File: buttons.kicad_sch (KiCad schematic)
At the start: 91 parts, among them SW1 TC002-N11AS2XT-RGB, SW10 TC002-N11AS2XT-RGB, SW11 TC002-N11AS2XT-RGB, SW12 TC002-N11AS2XT-RGB, SW13 TC002-N11AS2XT-RGB, SW2 TC002-N11AS2XT-RGB, SW3 TC002-N11AS2XT-RGB, SW4 TC002-N11AS2XT-RGB, SW5 TC002-N11AS2XT-RGB, SW6 TC002-N11AS2XT-RGB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

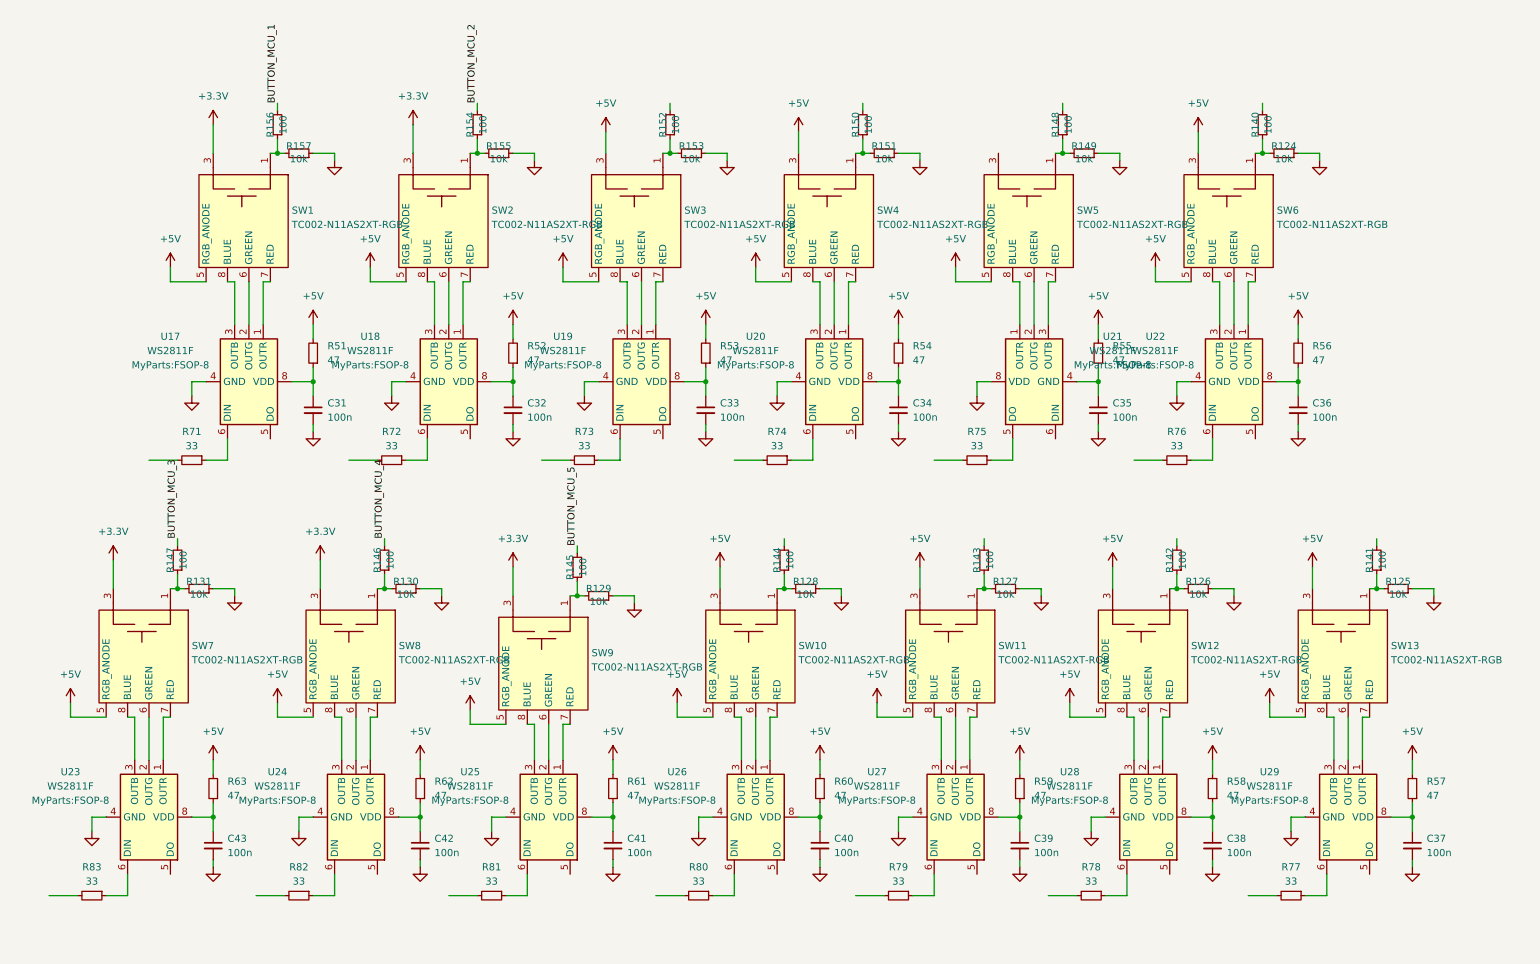
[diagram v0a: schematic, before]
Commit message: rename symbol & footprint libs
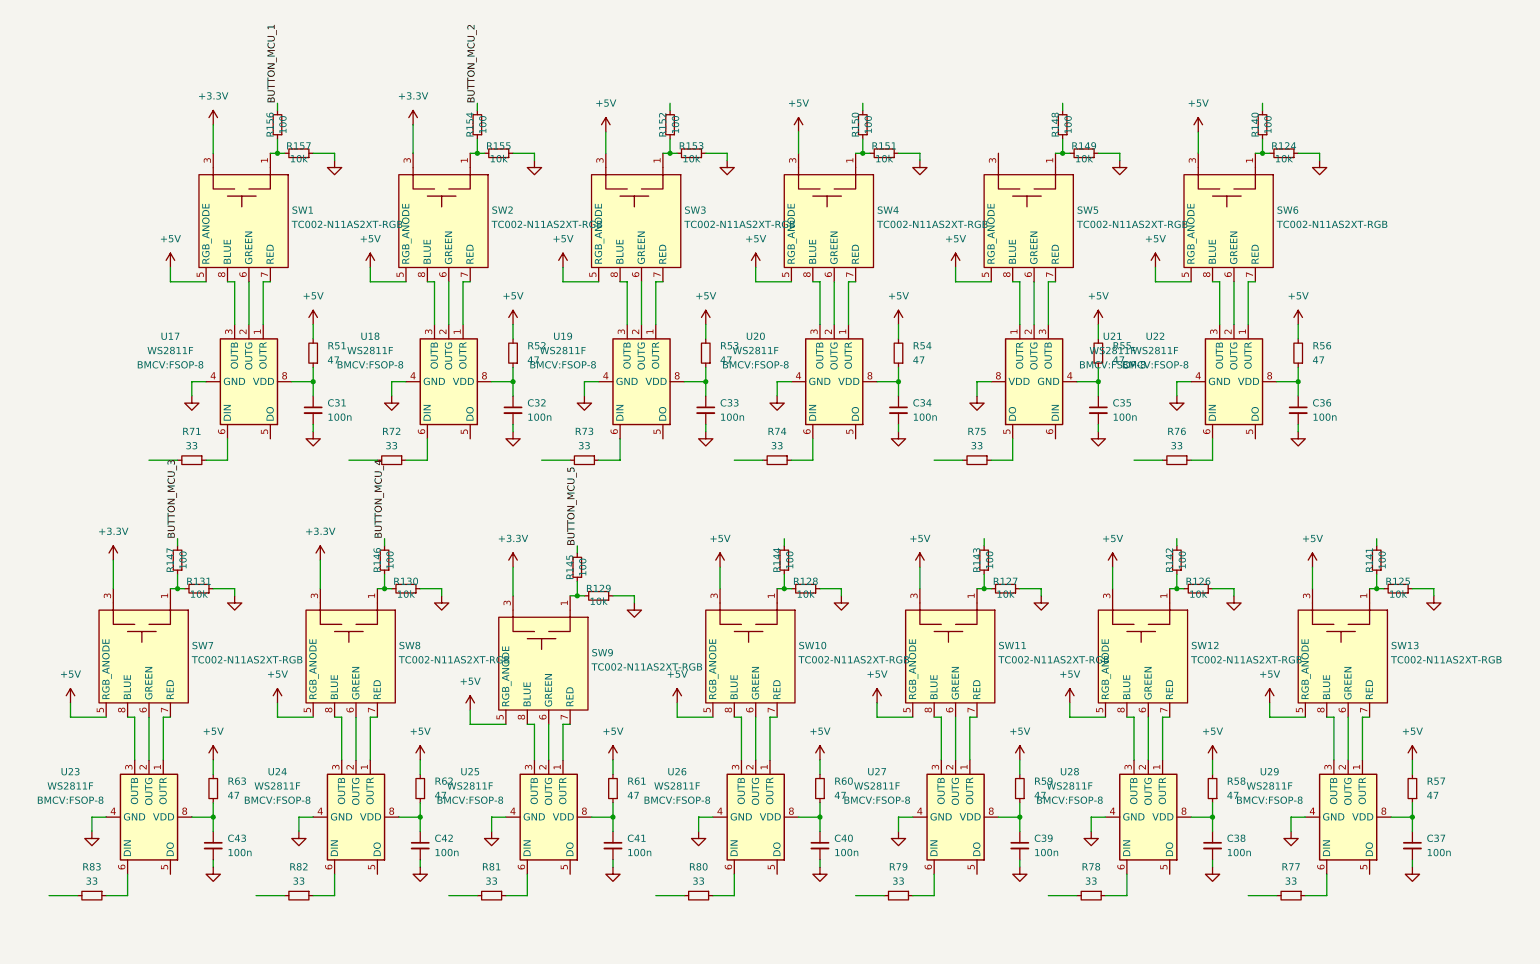
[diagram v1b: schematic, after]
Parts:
- SW1, SW10, SW11, SW12, SW13, SW2, SW3, SW4, SW5, SW6, SW7, SW8, SW9: footprint MyParts:TC002-N11AXXX-RGB -> BMCV:TC002-N11AXXX-RGB; symbol MySymbols:TC002-N11BXXX-RGB -> BMCV:TC002-N11BXXX-RGB
- U17, U18, U19, U20, U21, U22, U23, U24, U25, U26, U27, U28, U29: footprint MyParts:FSOP-8 -> BMCV:FSOP-8; symbol MySymbols:WS2811 -> BMCV:WS2811
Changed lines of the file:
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@@
 	)
 	(symbol
-		(lib_id "MySymbols:WS2811")
+		(lib_id "BMCV:WS2811")
 		(at 110.49 146.05 270)
 		(mirror x)
@@
 			)
 		)
-		(property "Footprint" "MyParts:FSOP-8"
+		(property "Footprint" "BMCV:FSOP-8"
 			(at 96.52 143.0938 90)
 			(effects
@@
 	)
 	(symbol
-		(lib_id "MySymbols:TC002-N11BXXX-RGB")
+		(lib_id "BMCV:TC002-N11BXXX-RGB")
 		(at 215.9 116.84 270)
 		(unit 1)
@@
 			)
 		)
-		(property "Footprint" "MyParts:TC002-N11AXXX-RGB"
+		(property "Footprint" "BMCV:TC002-N11AXXX-RGB"
 			(at 215.9 116.84 0)
 			(effects
@@
 	)
 	(symbol
-		(lib_id "MySymbols:TC002-N11BXXX-RGB")
+		(lib_id "BMCV:TC002-N11BXXX-RGB")
 		(at 251.46 116.84 270)
 		(unit 1)
@@
 			)
 		)
-		(property "Footprint" "MyParts:TC002-N11AXXX-RGB"
+		(property "Footprint" "BMCV:TC002-N11AXXX-RGB"
 			(at 251.46 116.84 0)
 			(effects
@@
 	)
 	(symbol
-		(lib_id "MySymbols:WS2811")
+		(lib_id "BMCV:WS2811")
 		(at 147.32 146.05 270)
 		(mirror x)
@@
 			)
 		)
-		(property "Footprint" "MyParts:FSOP-8"
+		(property "Footprint" "BMCV:FSOP-8"
 			(at 133.35 143.0938 90)
 			(effects
@@
 	)
 	(symbol
-		(lib_id "MySymbols:TC002-N11BXXX-RGB")
+		(lib_id "BMCV:TC002-N11BXXX-RGB")
 		(at 160.02 39.37 270)
 		(unit 1)
@@
 			)
 		)
-		(property "Footprint" "MyParts:TC002-N11AXXX-RGB"
+		(property "Footprint" "BMCV:TC002-N11AXXX-RGB"
 			(at 160.02 39.37 0)
 			(effects
@@
 	)
 	(symbol
-		(lib_id "MySymbols:TC002-N11BXXX-RGB")
+		(lib_id "BMCV:TC002-N11BXXX-RGB")
 		(at 55.88 39.37 270)
 		(unit 1)
@@
 			)
 		)
-		(property "Footprint" "MyParts:TC002-N11AXXX-RGB"
+		(property "Footprint" "BMCV:TC002-N11AXXX-RGB"
 			(at 55.88 39.37 0)
 			(effects
@@
 	)
 	(symbol
-		(lib_id "MySymbols:TC002-N11BXXX-RGB")
+		(lib_id "BMCV:TC002-N11BXXX-RGB")
 		(at 195.58 39.37 270)
 		(unit 1)
@@
 			)
 		)
-		(property "Footprint" "MyParts:TC002-N11AXXX-RGB"
+		(property "Footprint" "BMCV:TC002-N11AXXX-RGB"
 			(at 195.58 39.37 0)
 			(effects
@@
 	)
 	(symbol
-		(lib_id "MySymbols:WS2811")
+		(lib_id "BMCV:WS2811")
 		(at 39.37 146.05 270)
 		(mirror x)
@@
 			)
 		)
-		(property "Footprint" "MyParts:FSOP-8"
+		(property "Footprint" "BMCV:FSOP-8"
 			(at 25.4 143.0938 90)
 			(effects
@@
 	)
 	(symbol
-		(lib_id "MySymbols:TC002-N11BXXX-RGB")
+		(lib_id "BMCV:TC002-N11BXXX-RGB")
 		(at 146.05 116.84 270)
 		(unit 1)
@@
 			)
 		)
-		(property "Footprint" "MyParts:TC002-N11AXXX-RGB"
+		(property "Footprint" "BMCV:TC002-N11AXXX-RGB"
 			(at 146.05 116.84 0)
 			(effects
@@
 	)
 	(symbol
-		(lib_id "MySymbols:TC002-N11BXXX-RGB")
+		(lib_id "BMCV:TC002-N11BXXX-RGB")
 		(at 38.1 116.84 270)
 		(unit 1)
@@
 			)
 		)
-		(property "Footprint" "MyParts:TC002-N11AXXX-RGB"
+		(property "Footprint" "BMCV:TC002-N11AXXX-RGB"
 			(at 38.1 116.84 0)
 			(effects
@@
 	)
 	(symbol
-		(lib_id "MySymbols:WS2811")
+		(lib_id "BMCV:WS2811")
 		(at 217.17 146.05 270)
 		(mirror x)
@@
 			)
 		)
-		(property "Footprint" "MyParts:FSOP-8"
+		(property "Footprint" "BMCV:FSOP-8"
 			(at 203.2 143.0938 90)
 			(effects
@@
 	)
 	(symbol
-		(lib_id "MySymbols:TC002-N11BXXX-RGB")
+		(lib_id "BMCV:TC002-N11BXXX-RGB")
 		(at 74.93 116.84 270)
 		(unit 1)
@@
 			)
 		)
-		(property "Footprint" "MyParts:TC002-N11AXXX-RGB"
+		(property "Footprint" "BMCV:TC002-N11AXXX-RGB"
 			(at 74.93 116.84 0)
 			(effects
@@
 	)
 	(symbol
-		(lib_id "MySymbols:TC002-N11BXXX-RGB")
+		(lib_id "BMCV:TC002-N11BXXX-RGB")
 		(at 125.73 39.37 270)
 		(unit 1)
@@
 			)
 		)
-		(property "Footprint" "MyParts:TC002-N11AXXX-RGB"
+		(property "Footprint" "BMCV:TC002-N11AXXX-RGB"
 			(at 125.73 39.37 0)
 			(effects
@@
 	)
 	(symbol
-		(lib_id "MySymbols:WS2811")
+		(lib_id "BMCV:WS2811")
 		(at 161.29 68.58 270)
 		(mirror x)
@@
 			)
 		)
-		(property "Footprint" "MyParts:FSOP-8"
+		(property "Footprint" "BMCV:FSOP-8"
 			(at 147.32 65.6238 90)
 			(effects
@@
 	)
 	(symbol
-		(lib_id "MySymbols:WS2811")
+		(lib_id "BMCV:WS2811")
 		(at 92.71 68.58 270)
 		(mirror x)
@@
 			)
 		)
-		(property "Footprint" "MyParts:FSOP-8"
+		(property "Footprint" "BMCV:FSOP-8"
 			(at 78.74 65.6238 90)
 			(effects
@@
 	)
 	(symbol
-		(lib_id "MySymbols:TC002-N11BXXX-RGB")
+		(lib_id "BMCV:TC002-N11BXXX-RGB")
 		(at 181.61 116.84 270)
 		(unit 1)
@@
 			)
 		)
-		(property "Footprint" "MyParts:TC002-N11AXXX-RGB"
+		(property "Footprint" "BMCV:TC002-N11AXXX-RGB"
 			(at 181.61 116.84 0)
 			(effects
@@
 	)
 	(symbol
-		(lib_id "MySymbols:WS2811")
+		(lib_id "BMCV:WS2811")
 		(at 252.73 146.05 270)
 		(mirror x)
@@
 			)
 		)
-		(property "Footprint" "MyParts:FSOP-8"
+		(property "Footprint" "BMCV:FSOP-8"
 			(at 238.76 143.0938 90)
 			(effects
@@
 	)
 	(symbol
-		(lib_id "MySymbols:WS2811")
+		(lib_id "BMCV:WS2811")
 		(at 196.85 68.58 90)
 		(unit 1)
@@
 			)
 		)
-		(property "Footprint" "MyParts:FSOP-8"
+		(property "Footprint" "BMCV:FSOP-8"
 			(at 210.82 65.6238 90)
 			(effects
@@
 	)
 	(symbol
-		(lib_id "MySymbols:WS2811")
+		(lib_id "BMCV:WS2811")
 		(at 127 68.58 270)
 		(mirror x)
@@
 			)
 		)
-		(property "Footprint" "MyParts:FSOP-8"
+		(property "Footprint" "BMCV:FSOP-8"
 			(at 113.03 65.6238 90)
 			(effects
@@
 	)
 	(symbol
-		(lib_id "MySymbols:WS2811")
+		(lib_id "BMCV:WS2811")
 		(at 57.15 68.58 270)
 		(mirror x)
@@
 			)
 		)
-		(property "Footprint" "MyParts:FSOP-8"
+		(property "Footprint" "BMCV:FSOP-8"
 			(at 43.18 65.6238 90)
 			(effects
@@
 	)
 	(symbol
-		(lib_id "MySymbols:TC002-N11BXXX-RGB")
+		(lib_id "BMCV:TC002-N11BXXX-RGB")
 		(at 231.14 39.37 270)
 		(unit 1)
@@
 			)
 		)
-		(property "Footprint" "MyParts:TC002-N11AXXX-RGB"
+		(property "Footprint" "BMCV:TC002-N11AXXX-RGB"
 			(at 231.14 39.37 0)
 			(effects
@@
 	)
 	(symbol
-		(lib_id "MySymbols:WS2811")
+		(lib_id "BMCV:WS2811")
 		(at 76.2 146.05 270)
 		(mirror x)
@@
 			)
 		)
-		(property "Footprint" "MyParts:FSOP-8"
+		(property "Footprint" "BMCV:FSOP-8"
 			(at 62.23 143.0938 90)
 			(effects
@@
 	)
 	(symbol
-		(lib_id "MySymbols:TC002-N11BXXX-RGB")
+		(lib_id "BMCV:TC002-N11BXXX-RGB")
 		(at 109.22 118.11 270)
 		(unit 1)
@@
 			)
 		)
-		(property "Footprint" "MyParts:TC002-N11AXXX-RGB"
+		(property "Footprint" "BMCV:TC002-N11AXXX-RGB"
 			(at 109.22 118.11 0)
 			(effects
@@
 	)
 	(symbol
-		(lib_id "MySymbols:TC002-N11BXXX-RGB")
+		(lib_id "BMCV:TC002-N11BXXX-RGB")
 		(at 91.44 39.37 270)
 		(unit 1)
@@
 			)
 		)
-		(property "Footprint" "MyParts:TC002-N11AXXX-RGB"
+		(property "Footprint" "BMCV:TC002-N11AXXX-RGB"
 			(at 91.44 39.37 0)
 			(effects
@@
 	)
 	(symbol
-		(lib_id "MySymbols:WS2811")
+		(lib_id "BMCV:WS2811")
 		(at 182.88 146.05 270)
 		(mirror x)
@@
 			)
 		)
-		(property "Footprint" "MyParts:FSOP-8"
+		(property "Footprint" "BMCV:FSOP-8"
 			(at 168.91 143.0938 90)
 			(effects
@@
 	)
 	(symbol
-		(lib_id "MySymbols:WS2811")
+		(lib_id "BMCV:WS2811")
 		(at 232.41 68.58 270)
 		(mirror x)
@@
 			)
 		)
-		(property "Footprint" "MyParts:FSOP-8"
+		(property "Footprint" "BMCV:FSOP-8"
 			(at 218.44 65.6238 90)
 			(effects

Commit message: Routing WIP
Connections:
- net +3.3V: now also SW11.3, SW11.4, SW12.3, SW12.4, SW13.3, SW13.4, SW5.3, SW5.4, SW6.3, SW6.4; no longer SW1.3, SW1.4, SW2.3, SW2.4, SW7.3, SW7.4, SW8.3, SW8.4, SW9.3, SW9.4
- net +5V: now also SW1.3, SW1.4, SW2.3, SW2.4, SW7.3, SW7.4, SW8.3, SW8.4, SW9.3, SW9.4; no longer SW11.3, SW11.4, SW12.3, SW12.4, SW13.3, SW13.4, SW6.3, SW6.4
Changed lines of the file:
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@@
 	(wire
 		(pts
+			(xy 190.5 24.13) (xy 190.5 27.94)
+		)
+		(stroke
+			(width 0)
+			(type default)
+		)
+	)
+	(wire
+		(pts
 			(xy 104.14 66.04) (xy 104.14 68.58)
 		)
@@
 	(symbol
 		(lib_id "PCM_4ms_Power-symbol:+3.3V")
-		(at 104.14 101.6 0)
+		(at 210.82 101.6 0)
 		(unit 1)
 		(exclude_from_sim no)
@@
 		(fields_autoplaced yes)
 		(property "Reference" "#PWR0224"
-			(at 104.14 105.41 0)
+			(at 210.82 105.41 0)
 			(effects
 				(font
@@
 		)
 		(property "Value" "+3.3V"
-			(at 104.14 96.52 0)
+			(at 210.82 96.52 0)
 			(effects
 				(font
@@
 		)
 		(property "Footprint" ""
-			(at 104.14 101.6 0)
+			(at 210.82 101.6 0)
 			(effects
 				(font
@@
 		)
 		(property "Datasheet" ""
-			(at 104.14 101.6 0)
+			(at 210.82 101.6 0)
 			(effects
 				(font
@@
 		)
 		(property "Description" ""
-			(at 104.14 101.6 0)
+			(at 210.82 101.6 0)
 			(effects
 				(font
@@
 	)
 	(symbol
+		(lib_id "power:+5V")
+		(at 86.36 22.86 0)
+		(unit 1)
+		(exclude_from_sim no)
+		(in_bom yes)
+		(on_board yes)
+		(dnp no)
+		(fields_autoplaced yes)
+		(property "Reference" "#PWR0287"
+			(at 86.36 26.67 0)
+			(effects
+				(font
+					(size 1.27 1.27)
+				)
+				(hide yes)
+			)
+		)
+		(property "Value" "+5V"
+			(at 86.36 17.78 0)
+			(effects
+				(font
+					(size 1.27 1.27)
+				)
+			)
+		)
+		(property "Footprint" ""
+			(at 86.36 22.86 0)
+			(effects
+				(font
+					(size 1.27 1.27)
+				)
+				(hide yes)
+			)
+		)
+		(property "Datasheet" ""
+			(at 86.36 22.86 0)
+			(effects
+				(font
+					(size 1.27 1.27)
+				)
+				(hide yes)
+			)
+		)
+		(property "Description" "Power symbol creates a global label with name \"+5V\""
+			(at 86.36 22.86 0)
+			(effects
+				(font
+					(size 1.27 1.27)
+				)
+				(hide yes)
+			)
+		)
+		(pin "1"
+		)
+		(instances
+			(project "BMCV"
+				(path "/9b519346-c6ba-4bde-a176-1e9938a671fb/36ddee4d-206f-4ce8-ac32-91f0b23862f0"
+					(reference "#PWR0287")
+					(unit 1)
+				)
+			)
+		)
+	)
+	(symbol
 		(lib_id "power:GND")
 		(at 46.99 71.12 0)
@@
 	(symbol
 		(lib_id "power:+5V")
-		(at 226.06 24.13 0)
+		(at 50.8 22.86 0)
 		(unit 1)
 		(exclude_from_sim no)
@@
 		(fields_autoplaced yes)
 		(property "Reference" "#PWR0212"
-			(at 226.06 27.94 0)
+			(at 50.8 26.67 0)
 			(effects
 				(font
@@
 		)
 		(property "Value" "+5V"
-			(at 226.06 19.05 0)
+			(at 50.8 17.78 0)
 			(effects
 				(font
@@
 		)
 		(property "Footprint" ""
-			(at 226.06 24.13 0)
+			(at 50.8 22.86 0)
 			(effects
 				(font
@@
 		)
 		(property "Datasheet" ""
-			(at 226.06 24.13 0)
+			(at 50.8 22.86 0)
 			(effects
 				(font
@@
 		)
 		(property "Description" "Power symbol creates a global label with name \"+5V\""
-			(at 226.06 24.13 0)
+			(at 50.8 22.86 0)
 			(effects
 				(font
@@
 	(symbol
 		(lib_id "PCM_4ms_Power-symbol:+3.3V")
-		(at 69.85 100.33 0)
+		(at 190.5 24.13 0)
 		(unit 1)
 		(exclude_from_sim no)
@@
 		(fields_autoplaced yes)
 		(property "Reference" "#PWR0222"
-			(at 69.85 104.14 0)
+			(at 190.5 27.94 0)
 			(effects
 				(font
@@
 		)
 		(property "Value" "+3.3V"
-			(at 69.85 95.25 0)
+			(at 190.5 19.05 0)
 			(effects
 				(font
@@
 		)
 		(property "Footprint" ""
-			(at 69.85 100.33 0)
+			(at 190.5 24.13 0)
 			(effects
 				(font
@@
 		)
 		(property "Datasheet" ""
-			(at 69.85 100.33 0)
+			(at 190.5 24.13 0)
 			(effects
 				(font
@@
 		)
 		(property "Description" ""
-			(at 69.85 100.33 0)
+			(at 190.5 24.13 0)
 			(effects
 				(font
@@
 	(symbol
 		(lib_id "PCM_4ms_Power-symbol:+3.3V")
-		(at 86.36 22.86 0)
+		(at 246.38 101.6 0)
 		(unit 1)
 		(exclude_from_sim no)
@@
 		(fields_autoplaced yes)
 		(property "Reference" "#PWR0232"
-			(at 86.36 26.67 0)
+			(at 246.38 105.41 0)
 			(effects
 				(font
@@
 		)
 		(property "Value" "+3.3V"
-			(at 86.36 17.78 0)
+			(at 246.38 96.52 0)
 			(effects
 				(font
@@
 		)
 		(property "Footprint" ""
-			(at 86.36 22.86 0)
+			(at 246.38 101.6 0)
 			(effects
 				(font
@@
 		)
 		(property "Datasheet" ""
-			(at 86.36 22.86 0)
+			(at 246.38 101.6 0)
 			(effects
 				(font
@@
 		)
 		(property "Description" ""
-			(at 86.36 22.86 0)
+			(at 246.38 101.6 0)
 			(effects
 				(font
@@
 	(symbol
 		(lib_id "power:+5V")
-		(at 176.53 101.6 0)
+		(at 69.85 100.33 0)
 		(unit 1)
 		(exclude_from_sim no)
@@
 		(fields_autoplaced yes)
 		(property "Reference" "#PWR0216"
-			(at 176.53 105.41 0)
+			(at 69.85 104.14 0)
 			(effects
 				(font
@@
 		)
 		(property "Value" "+5V"
-			(at 176.53 96.52 0)
+			(at 69.85 95.25 0)
 			(effects
 				(font
@@
 		)
 		(property "Footprint" ""
-			(at 176.53 101.6 0)
+			(at 69.85 100.33 0)
 			(effects
 				(font
@@
 		)
 		(property "Datasheet" ""
-			(at 176.53 101.6 0)
+			(at 69.85 100.33 0)
 			(effects
 				(font
@@
 		)
 		(property "Description" "Power symbol creates a global label with name \"+5V\""
-			(at 176.53 101.6 0)
+			(at 69.85 100.33 0)
 			(effects
 				(font
@@
 	(symbol
 		(lib_id "power:+5V")
-		(at 246.38 101.6 0)
+		(at 104.14 101.6 0)
 		(unit 1)
 		(exclude_from_sim no)
@@
 		(fields_autoplaced yes)
 		(property "Reference" "#PWR0210"
-			(at 246.38 105.41 0)
+			(at 104.14 105.41 0)
 			(effects
 				(font
@@
 		)
 		(property "Value" "+5V"
-			(at 246.38 96.52 0)
+			(at 104.14 96.52 0)
 			(effects
 				(font
@@
 		)
 		(property "Footprint" ""
-			(at 246.38 101.6 0)
+			(at 104.14 101.6 0)
 			(effects
 				(font
@@
 		)
 		(property "Datasheet" ""
-			(at 246.38 101.6 0)
+			(at 104.14 101.6 0)
 			(effects
 				(font
@@
 		)
 		(property "Description" "Power symbol creates a global label with name \"+5V\""
-			(at 246.38 101.6 0)
+			(at 104.14 101.6 0)
 			(effects
 				(font
@@
 	(symbol
 		(lib_id "PCM_4ms_Power-symbol:+3.3V")
-		(at 50.8 22.86 0)
+		(at 226.06 24.13 0)
 		(unit 1)
 		(exclude_from_sim no)
@@
 		(fields_autoplaced yes)
 		(property "Reference" "#PWR0231"
-			(at 50.8 26.67 0)
+			(at 226.06 27.94 0)
 			(effects
 				(font
@@
 		)
 		(property "Value" "+3.3V"
-			(at 50.8 17.78 0)
+			(at 226.06 19.05 0)
 			(effects
 				(font
@@
 		)
 		(property "Footprint" ""
-			(at 50.8 22.86 0)
+			(at 226.06 24.13 0)
 			(effects
 				(font
@@
 		)
 		(property "Datasheet" ""
-			(at 50.8 22.86 0)
+			(at 226.06 24.13 0)
 			(effects
 				(font
@@
 		)
 		(property "Description" ""
-			(at 50.8 22.86 0)
+			(at 226.06 24.13 0)
 			(effects
 				(font
@@
 	(symbol
 		(lib_id "power:+5V")
-		(at 210.82 101.6 0)
+		(at 33.02 100.33 0)
 		(unit 1)
 		(exclude_from_sim no)
@@
 		(fields_autoplaced yes)
 		(property "Reference" "#PWR0214"
-			(at 210.82 105.41 0)
+			(at 33.02 104.14 0)
 			(effects
 				(font
@@
 		)
 		(property "Value" "+5V"
-			(at 210.82 96.52 0)
+			(at 33.02 95.25 0)
 			(effects
 				(font
@@
 		)
 		(property "Footprint" ""
-			(at 210.82 101.6 0)
+			(at 33.02 100.33 0)
 			(effects
 				(font
@@
 		)
 		(property "Datasheet" ""
-			(at 210.82 101.6 0)
+			(at 33.02 100.33 0)
 			(effects
 				(font
@@
 		)
 		(property "Description" "Power symbol creates a global label with name \"+5V\""
-			(at 210.82 101.6 0)
+			(at 33.02 100.33 0)
 			(effects
 				(font
@@
 	(symbol
 		(lib_id "PCM_4ms_Power-symbol:+3.3V")
-		(at 33.02 100.33 0)
+		(at 176.53 101.6 0)
 		(unit 1)
 		(exclude_from_sim no)
@@
 		(fields_autoplaced yes)
 		(property "Reference" "#PWR0220"
-			(at 33.02 104.14 0)
+			(at 176.53 105.41 0)
 			(effects
 				(font
@@
 		)
 		(property "Value" "+3.3V"
-			(at 33.02 95.25 0)
+			(at 176.53 96.52 0)
 			(effects
 				(font
@@
 		)
 		(property "Footprint" ""
-			(at 33.02 100.33 0)
+			(at 176.53 101.6 0)
 			(effects
 				(font
@@
 		)
 		(property "Datasheet" ""
-			(at 33.02 100.33 0)
+			(at 176.53 101.6 0)
 			(effects
 				(font
@@
 		)
 		(property "Description" ""
-			(at 33.02 100.33 0)
+			(at 176.53 101.6 0)
 			(effects
 				(font
